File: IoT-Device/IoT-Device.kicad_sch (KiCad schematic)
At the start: 47 parts, among them J1 USB-C, J2 Conn_01x02, J3 SWD, SW1 RESET, SW2 BOOT_MODE, U1 BD33GA5WEFJ, U2 STM32U585VI, U3 BQ24074RGT, U4 ESP32-C3-WROOM-02

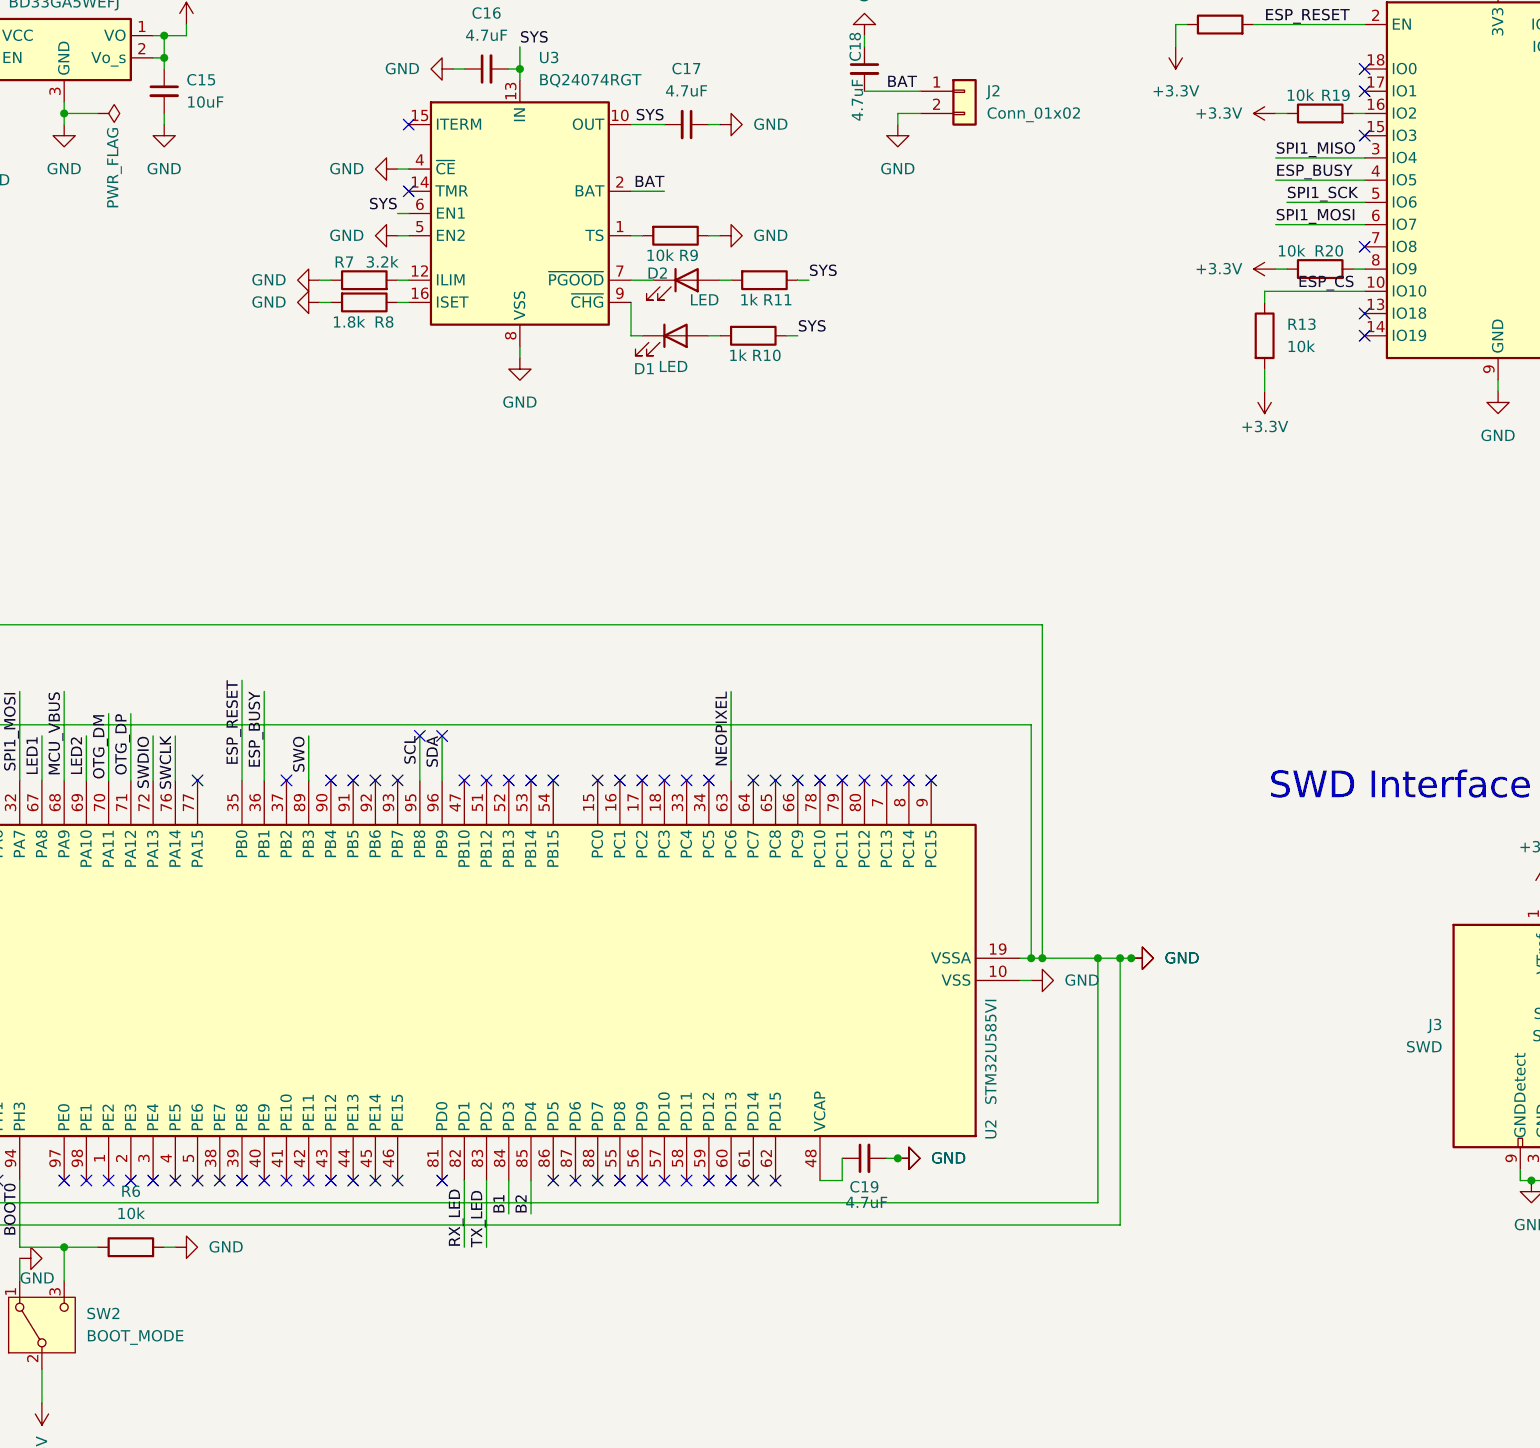
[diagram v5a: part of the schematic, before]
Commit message: update schematic and PCB to allow ESP32-C3 boot mode change via STM32
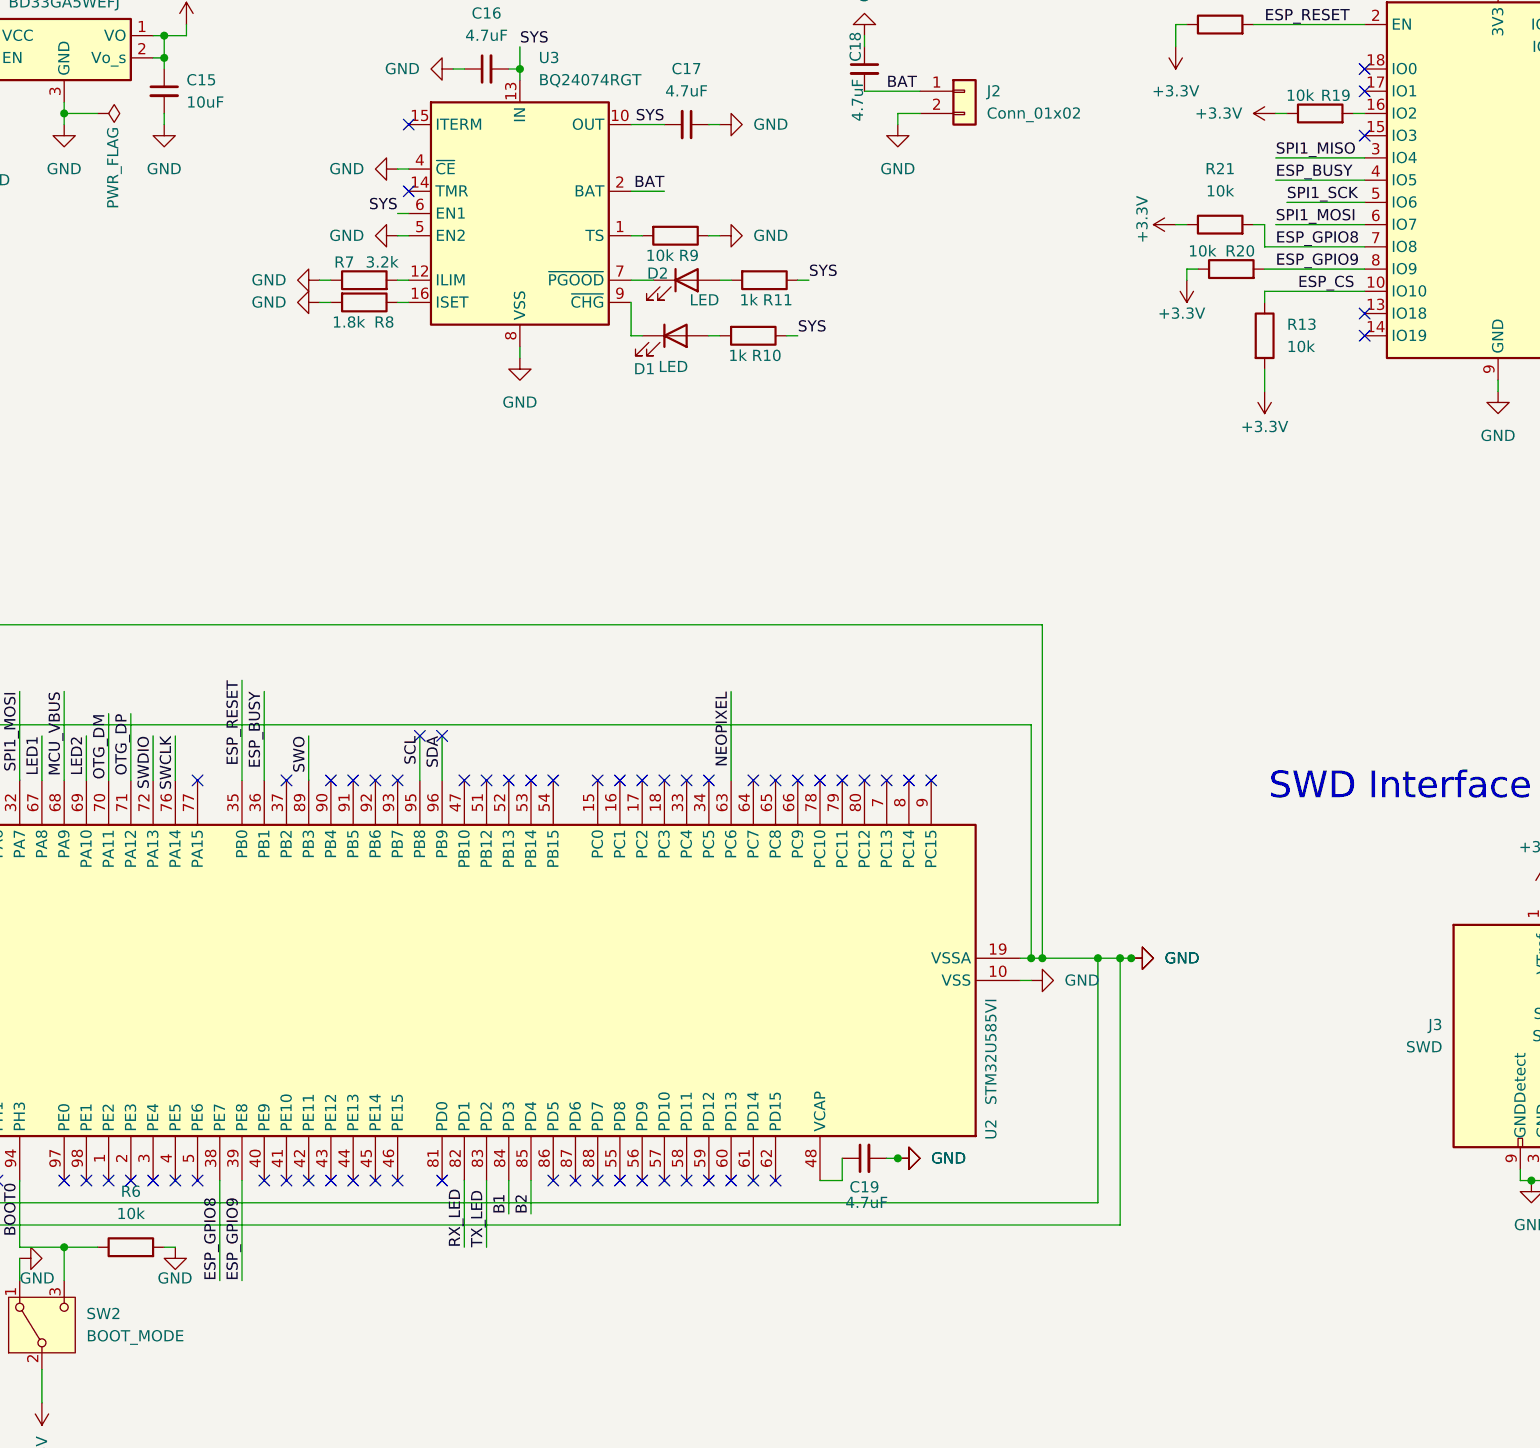
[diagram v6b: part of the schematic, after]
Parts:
- added R21: 10k, Resistor_SMD:R_0603_1608Metric, symbol Device:R
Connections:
- net +3.3V: now also R21.1
- net ESP_GPIO8: now reaches U2.38 (PE7)
- net ESP_GPIO8: now also U4.7 (IO8), R21.2
- net ESP_GPIO9: now reaches U2.39 (PE8)
- net ESP_GPIO9: now also R20.2, U4.8 (IO9)
- no-connect marks 71 -> 68
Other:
- moved on the sheet: R20

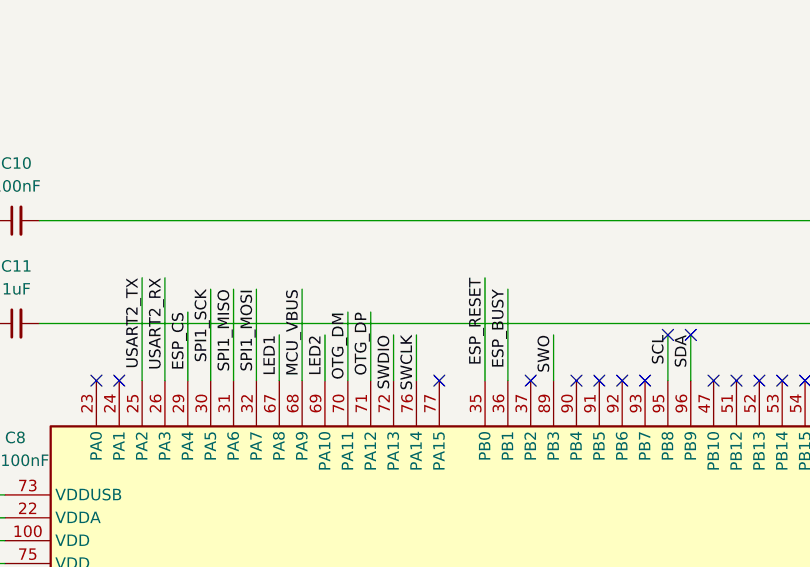
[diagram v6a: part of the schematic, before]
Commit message: change two ESP32 pins for slightly more appropriate ones on STM32 (ESP_BUSY->PB2 (SPI1_RDY)
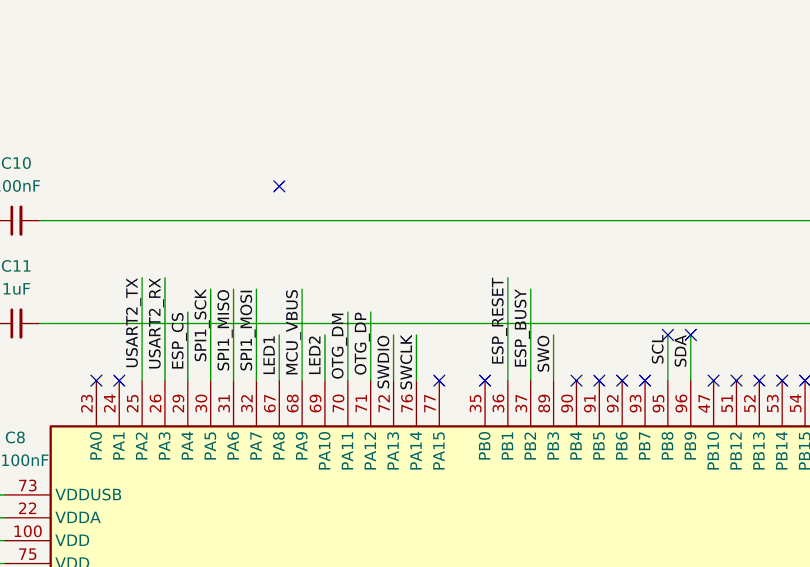
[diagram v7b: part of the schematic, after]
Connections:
- net ESP_BUSY: now also U2.37 (PB2); no longer U2.36 (PB1)
- net ESP_RESET: now also U2.36 (PB1); no longer U2.35 (PB0)
- no-connect marks 68 -> 69
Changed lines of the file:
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@@
-	)
-	(no_connect
-		(at 115.57 114.3)
 	)
 	(no_connect
@@
 	)
 	(no_connect
+		(at 110.49 114.3)
+	)
+	(no_connect
 		(at 140.97 114.3)
+	)
+	(no_connect
+		(at 87.63 92.71)
 	)
 	(no_connect
@@
 	(wire
 		(pts
+			(xy 115.57 104.14) (xy 115.57 114.3)
+		)
+		(stroke
+			(width 0)
+			(type default)
+		)
+	)
+	(wire
+		(pts
 			(xy 72.39 160.02) (xy 72.39 165.1)
 		)
@@
 	(wire
 		(pts
-			(xy 113.03 104.14) (xy 113.03 114.3)
+			(xy 113.03 102.87) (xy 113.03 114.3)
 		)
 		(stroke
@@
 		(pts
 			(xy 163.83 52.07) (xy 165.1 52.07)
-		)
-		(stroke
-			(width 0)
-			(type default)
-		)
-	)
-	(wire
-		(pts
-			(xy 110.49 102.87) (xy 110.49 114.3)
 		)
 		(stroke
@@
 	)
 	(label "ESP_RESET"
-		(at 110.49 102.87 270)
+		(at 113.03 102.87 270)
 		(effects
 			(font
@@
 	)
 	(label "ESP_BUSY"
-		(at 113.03 104.14 270)
-		(effects
-			(font
+		(at 115.57 104.14 270)
+		(effects
+			(font

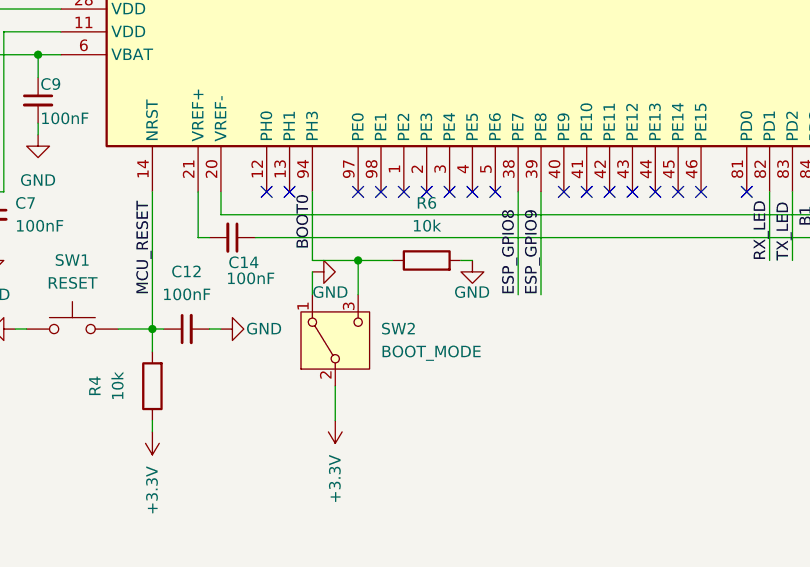
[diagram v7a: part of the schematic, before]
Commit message: update SW2 GND routing
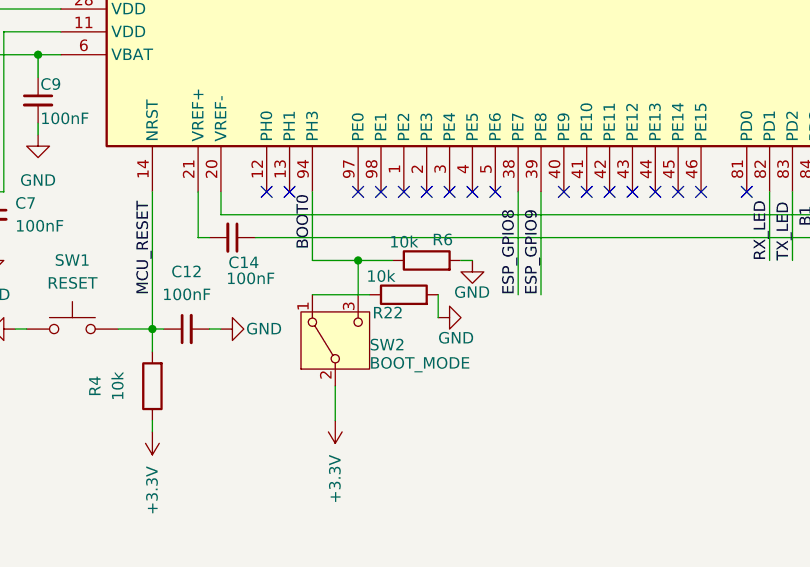
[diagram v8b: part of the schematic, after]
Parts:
- added R22: 10k, Resistor_SMD:R_0603_1608Metric, symbol Device:R
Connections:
- net GND: now also R22.2; no longer SW2.1 (A)
- new net: R22.1, SW2.1 (A)
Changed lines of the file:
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@@
 	(wire
 		(pts
+			(xy 85.09 171.45) (xy 91.44 171.45)
+		)
+		(stroke
+			(width 0)
+			(type default)
+		)
+	)
+	(wire
+		(pts
 			(xy 72.39 160.02) (xy 72.39 165.1)
 		)
@@
 	(wire
 		(pts
-			(xy 85.09 168.91) (xy 85.09 171.45)
-		)
-		(stroke
-			(width 0)
-			(type default)
-		)
-	)
-	(wire
-		(pts
 			(xy 201.93 134.62) (xy 200.66 134.62)
 		)
@@
 	(wire
 		(pts
+			(xy 99.06 171.45) (xy 99.06 173.99)
+		)
+		(stroke
+			(width 0)
+			(type default)
+		)
+	)
+	(wire
+		(pts
 			(xy 217.17 27.94) (xy 218.44 27.94)
 		)
@@
 	)
 	(symbol
+		(lib_id "Device:R")
+		(at 95.25 171.45 90)
+		(unit 1)
+		(exclude_from_sim no)
+		(in_bom yes)
+		(on_board yes)
+		(dnp no)
+		(property "Reference" "R22"
+			(at 93.472 173.482 90)
+			(effects
+				(font
+					(size 1.27 1.27)
+				)
+			)
+		)
+		(property "Value" "10k"
+			(at 92.71 169.418 90)
+			(effects
+				(font
+					(size 1.27 1.27)
+				)
+			)
+		)
+		(property "Footprint" "Resistor_SMD:R_0603_1608Metric"
+			(at 95.25 173.228 90)
+			(effects
+				(font
+					(size 1.27 1.27)
+				)
+				(hide yes)
+			)
+		)
+		(property "Datasheet" "~"
+			(at 95.25 171.45 0)
+			(effects
+				(font
+					(size 1.27 1.27)
+				)
+				(hide yes)
+			)
+		)
+		(property "Description" "Resistor"
+			(at 95.25 171.45 0)
+			(effects
+				(font
+					(size 1.27 1.27)
+				)
+				(hide yes)
+			)
+		)
+		(pin "2"
+		)
+		(pin "1"
+		)
+		(instances
+			(project "IoT-Device"
+				(path "/c28d0510-3574-42bd-a404-b115c4b1ce64"
+					(reference "R22")
+					(unit 1)
+				)
+			)
+		)
+	)
+	(symbol
 		(lib_id "power:GND")
 		(at 185.42 39.37 0)
@@
 		(on_board yes)
 		(dnp no)
-		(fields_autoplaced yes)
 		(property "Reference" "SW2"
-			(at 92.71 175.2599 90)
+			(at 91.44 177.038 90)
 			(effects
 				(font
@@
 		)
 		(property "Value" "BOOT_MODE"
-			(at 92.71 177.7999 90)
+			(at 91.44 179.07 90)
 			(effects
 				(font
@@
 	(symbol
 		(lib_id "power:GND")
-		(at 85.09 168.91 90)
+		(at 99.06 173.99 90)
 		(unit 1)
 		(exclude_from_sim no)
@@
 		(dnp no)
 		(property "Reference" "#PWR020"
-			(at 91.44 168.91 0)
+			(at 105.41 173.99 0)
 			(effects
 				(font
@@
 		)
 		(property "Value" "GND"
-			(at 85.09 171.196 90)
+			(at 99.06 176.276 90)
 			(effects
 				(font
@@
 		)
 		(property "Footprint" ""
-			(at 85.09 168.91 0)
+			(at 99.06 173.99 0)
 			(effects
 				(font
@@
 		)
 		(property "Datasheet" ""
-			(at 85.09 168.91 0)
+			(at 99.06 173.99 0)
 			(effects
 				(font
@@
 		)
 		(property "Description" "Power symbol creates a global label with name \"GND\" , ground"
-			(at 85.09 168.91 0)
+			(at 99.06 173.99 0)
 			(effects
 				(font
@@
 		(on_board yes)
 		(dnp no)
-		(fields_autoplaced yes)
 		(property "Reference" "R6"
-			(at 97.79 161.29 90)
+			(at 99.568 165.354 90)
 			(effects
 				(font
@@
 		)
 		(property "Value" "10k"
-			(at 97.79 163.83 90)
+			(at 95.25 165.608 90)
 			(effects
 				(font
